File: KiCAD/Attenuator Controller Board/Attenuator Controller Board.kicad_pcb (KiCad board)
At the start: 2 copper layers, 100 x 70 mm, 30 parts, among them J1 Barrel_Jack_Switch, J2 Conn_Coaxial, J3 Conn_Coaxial, J4 Conn_01x24_Female, J5 DSub_15_HD, J6 DSub9, J7 DSub9, J8 DSub9, J9 Conn_01x24_Female, U1 RU_28_ADI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

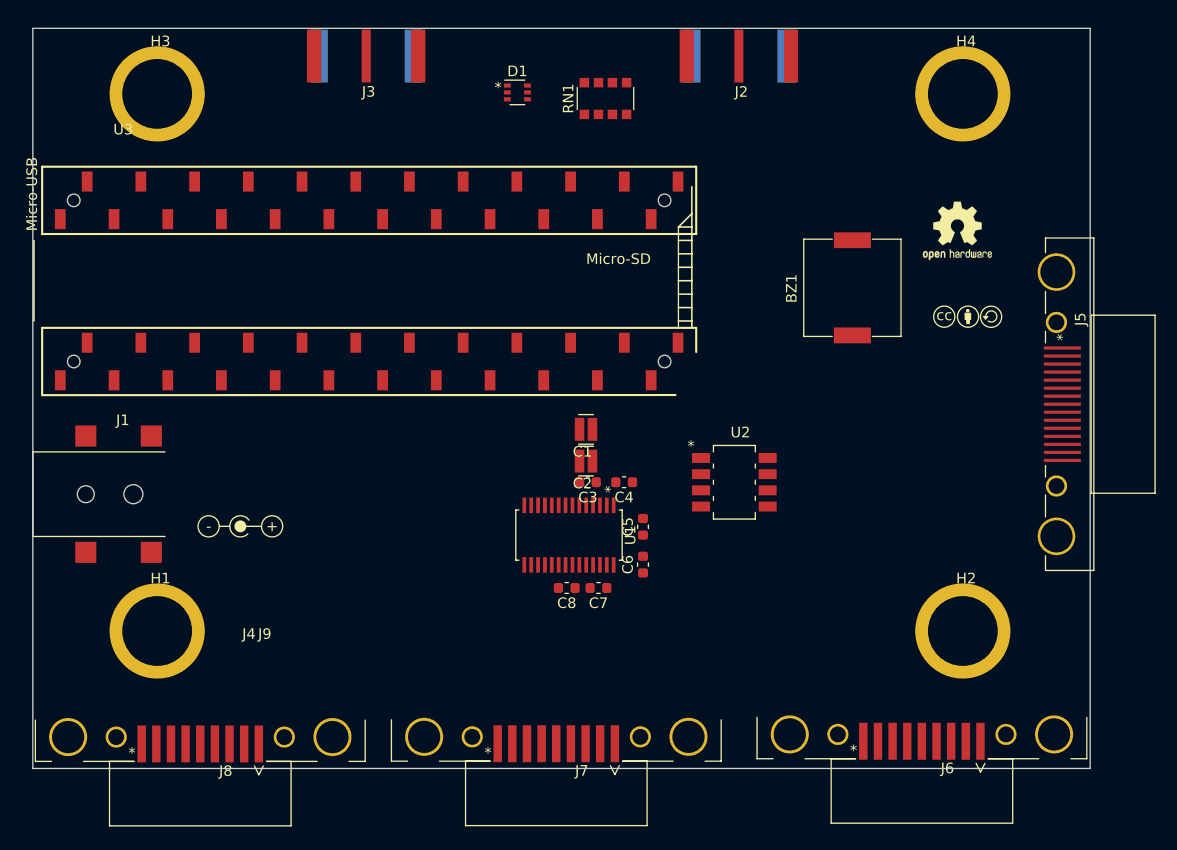
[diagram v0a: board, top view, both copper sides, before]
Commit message: Schottky diode protecting Vin->motor added
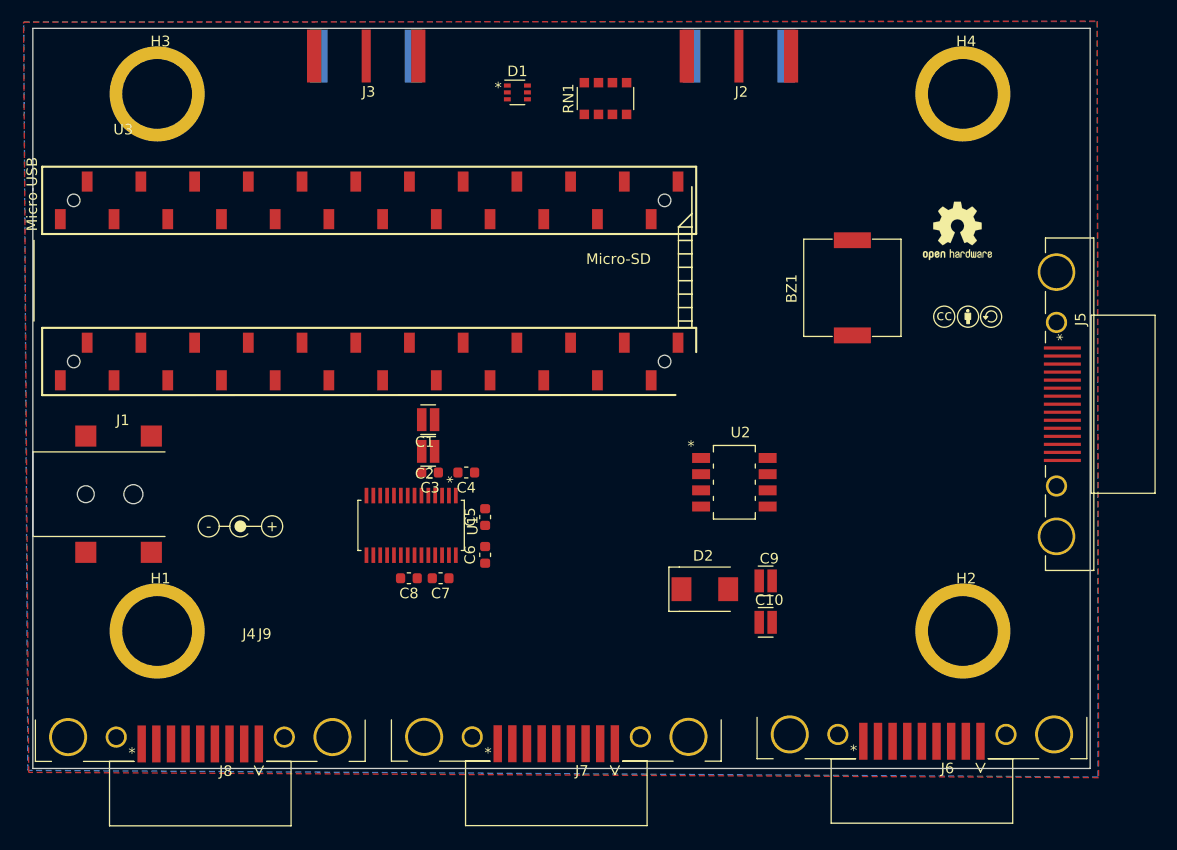
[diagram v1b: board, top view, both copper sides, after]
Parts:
- added C10: 10µF, Custom Footprints:0508_Capacitor, F.Cu at (169.3, 126.2)
- added C9: 10µF, Custom Footprints:0508_Capacitor, F.Cu at (169.3, 122.3)
- added D2: D_Schottky, Custom Footprints:DO-214BA, F.Cu at (163.6, 123.0)
- moved C1 15.0 mm to (137.4, 107.0)
- moved C2 15.0 mm to (137.4, 110.0)
- moved C3 15.0 mm to (137.6, 112.0)
- moved C4 15.0 mm to (141.0, 112.0)
- moved C5 15.0 mm to (142.8, 116.2)
- moved C6 15.0 mm to (142.8, 119.8)
- moved C7 15.0 mm to (138.6, 122.0)
- moved C8 15.0 mm to (135.6, 122.0)
- moved U1 15.0 mm to (135.8, 117.0)
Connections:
- U2 pad 6: /5V -> Net-(C10-Pad1)
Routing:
- added copper zone on B.Cu, net GND
- added copper zone on F.Cu, net GND

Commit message: Started on traces
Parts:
- U1: value RU_28_ADI -> ADM3307EARUZ
- U2: value SOIC_7T8TA_DIO -> ZXMHC3A01T8TA
- moved J8 68.3 mm to (184.1, 139.3)
- moved J6 68.2 mm to (115.9, 139.3)
- moved C1 4.34 mm to (137.6, 111.3)
- moved C4 4.28 mm to (139.9, 116.2)
- moved C3 4.19 mm to (137.0, 116.2)
- moved C2 4.05 mm to (137.6, 114.1)
- moved C5 3.98 mm to (140.8, 119.7)
- moved U1 3.80 mm to (134.9, 120.7)
- moved C6 3.49 mm to (140.8, 122.7), turned to 270 degrees
- moved C7 3.26 mm to (138.7, 125.3)
- moved C8 3.25 mm to (135.7, 125.3)
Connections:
- U1 pad 15: /RS-232_RXD3 -> /RS-232_RXD1
- U1 pad 17: /RS-232_RXD1 -> /RS-232_RXD3
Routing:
- net GND: track 0.00 -> 54.1 mm
- net /5V: track 0.00 -> 30.7 mm
- net /Gate3-4: track 0.00 -> 20.8 mm
- net /Gate1-2: track 0.00 -> 19.6 mm
- net /3v3: track 0.00 -> 16.4 mm
- net Net-(C6-Pad2): track 0.00 -> 10.3 mm
- net Net-(C5-Pad1): track 0.00 -> 5.25 mm
- net Net-(C5-Pad2): track 0.00 -> 4.20 mm
- net Net-(C6-Pad1): track 0.00 -> 4.19 mm
- net Net-(C4-Pad1): track 0.00 -> 2.39 mm
- net Net-(C7-Pad1): track 0.00 -> 2.15 mm
- net Net-(C7-Pad2): track 0.00 -> 2.03 mm
- net Net-(C8-Pad1): track 0.00 -> 1.76 mm

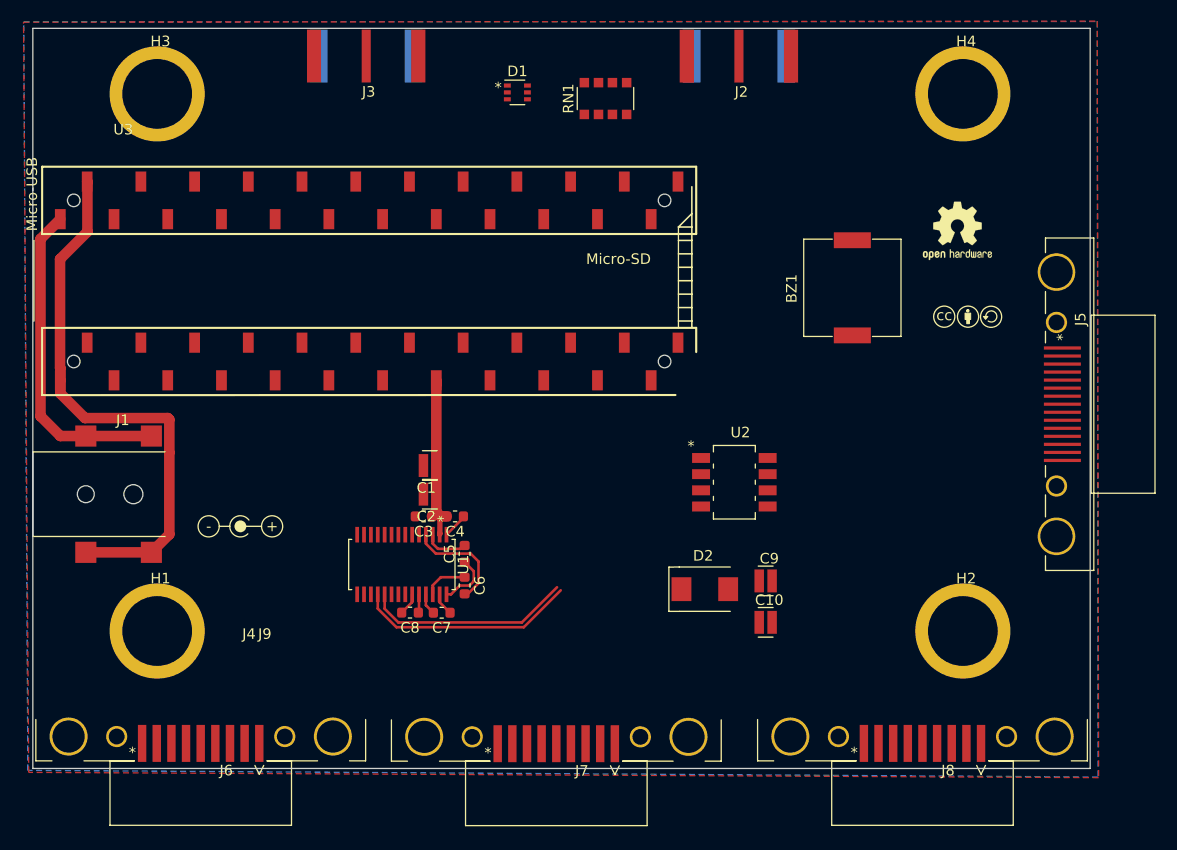
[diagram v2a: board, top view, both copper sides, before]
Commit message: RS-232 outs connected and shielded
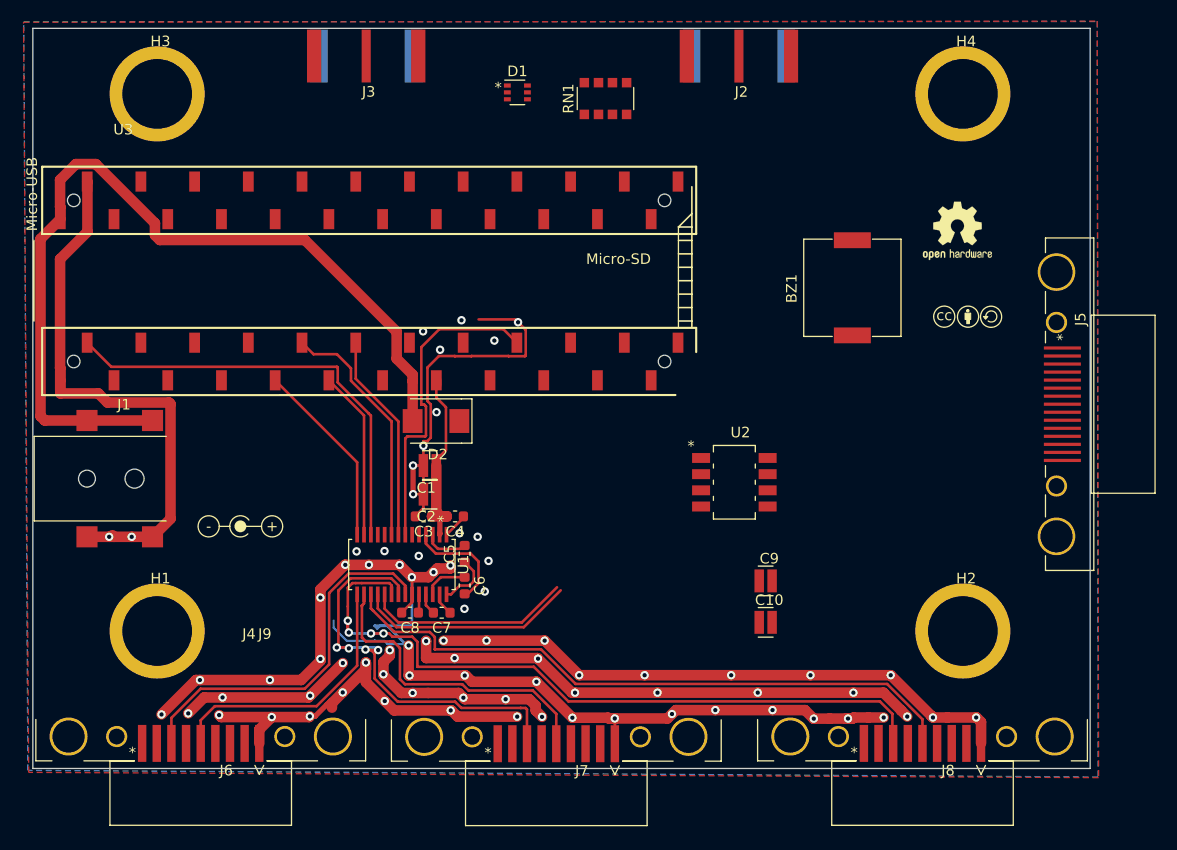
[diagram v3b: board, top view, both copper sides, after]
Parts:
- moved D2 30.0 mm to (138.1, 107.1), turned to 180 degrees
- moved J1 1.47 mm to (100.1, 112.6)
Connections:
- U3 pad 19: /Serial1-RX -> /NC27
- U3 pad 2: /Gate1-2 -> /Serial1-RX
- U3 pad 21: /NC29 -> /Enable
- U3 pad 22: /NC30 -> /Shutdown
- U3 pad 3: /Gate3-4 -> /NC1
- U3 pad 4: /Enable -> Net-(J4-Pad~)
- U3 pad 5: /Shutdown -> /Motor1
- U3 pad 7: /Encoder(A) -> /Motor2
- U3 pad 8: /Encoder(B) -> Net-(J4-Pad~)
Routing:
- net GND: track 54.1 -> 383.1 mm, vias 0 -> 78
- net /RS-232_TXD3: track 0.00 -> 72.0 mm, vias 0 -> 4
- net /RS-232_RXD3: track 0.00 -> 60.8 mm
- net /5V: track 30.7 -> 82.7 mm
- net /RS-232_TXD2: track 0.00 -> 42.3 mm, vias 0 -> 4
- net /Serial1-RX: track 0.00 -> 41.8 mm
- net /RS-232_TXD1: track 0.00 -> 35.4 mm
- net /RS-232_RXD2: track 0.00 -> 30.2 mm
- net /Serial1-TX: track 0.00 -> 30.1 mm
- net /RS-232_RXD1: track 0.00 -> 25.9 mm
- net /Serial3-TX: track 0.00 -> 23.0 mm
- net /Serial2-TX: track 0.00 -> 19.8 mm
- net /Serial3-RX: track 0.00 -> 17.8 mm
- net /Serial2-RX: track 0.00 -> 16.0 mm
- net /3v3: track 16.4 -> 18.5 mm

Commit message: Keep SD and EN low to keep RS-232 driver always on
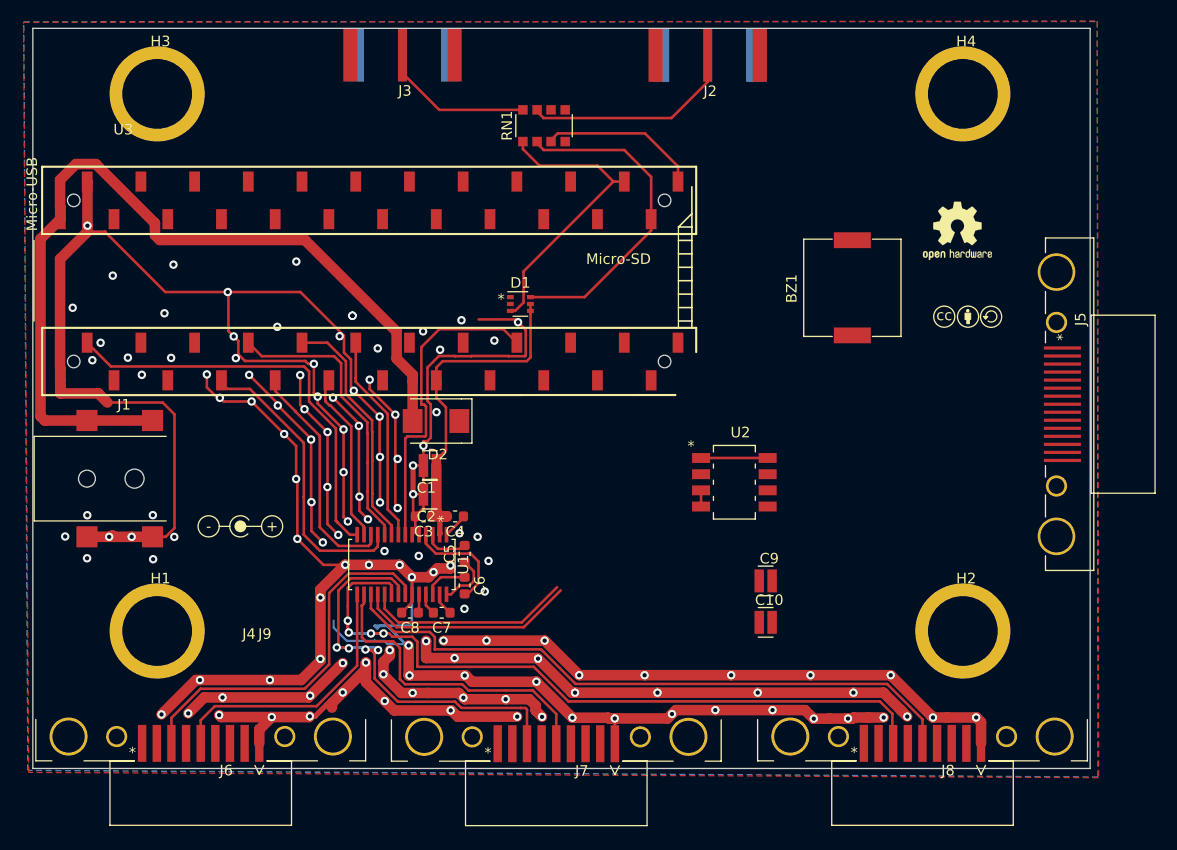
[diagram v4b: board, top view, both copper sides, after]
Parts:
- moved D1 20.0 mm to (146.1, 96.1)
- moved RN1 6.35 mm to (148.3, 79.2)
- moved J3 3.43 mm to (135.0, 72.5)
- moved J2 2.95 mm to (163.8, 72.6)
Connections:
- D1 pad 4: /3.3V -> /3v3
- D1 pad 5: /3.3V -> /3v3
- RN1 pad 1: /Analog_Input1 -> /Analog_Input2
- RN1 pad 2: /Analog_Input2 -> /Analog_Input1
- RN1 pad 3: GND -> /Ident(-)
- RN1 pad 6: /Ident(-) -> GND
- RN1 pad 7: Net-(J3-Pad1) -> Net-(J2-Pad1)
- RN1 pad 8: Net-(J2-Pad1) -> Net-(J3-Pad1)
- U1 pad 12: /Serial1-RX -> /Serial3-RX
- U1 pad 14: /Serial3-RX -> /Serial1-RX
- U1 pad 5: /Enable -> GND
- U1 pad 6: /Shutdown -> GND
- U3 pad 21: /Enable -> GND
- U3 pad 22: /Shutdown -> GND
- U3 pad 23: /Ident(-) -> Net-(J4-Pad~)
- U3 pad 24: /Analog_Input2 -> Net-(J4-Pad~)
- U3 pad 30: /Analog_Input1 -> /Ident(-)
- U3 pad 31: /NC34 -> /Analog_Input1
- U3 pad 32: /NC35 -> /Analog_Input2
- U3 pad 4: Net-(J4-Pad~) -> /NC2
- U3 pad 5: /Motor1 -> /NC3
- U3 pad 8: Net-(J4-Pad~) -> /Motor1
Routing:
- net GND: track 383.1 -> 552.3 mm, vias 78 -> 135
- net /Analog_Input1: track 0.00 -> 31.4 mm
- net /Analog_Input2: track 0.00 -> 28.1 mm
- net /Motor2: track 0.00 -> 28.0 mm
- net /Motor1: track 0.00 -> 27.5 mm
- net Net-(J2-Pad1): track 0.00 -> 20.5 mm
- net /3v3: track 18.5 -> 34.6 mm
- net /Ident(-): track 0.00 -> 15.1 mm
- net Net-(J3-Pad1): track 0.00 -> 14.5 mm
- net /Gate3-4: track 20.8 -> 27.1 mm
- net /Serial3-RX: track 17.8 -> 22.2 mm
- net /Serial1-RX: track 41.8 -> 40.1 mm
- net /Gate1-2: track 19.6 -> 21.1 mm

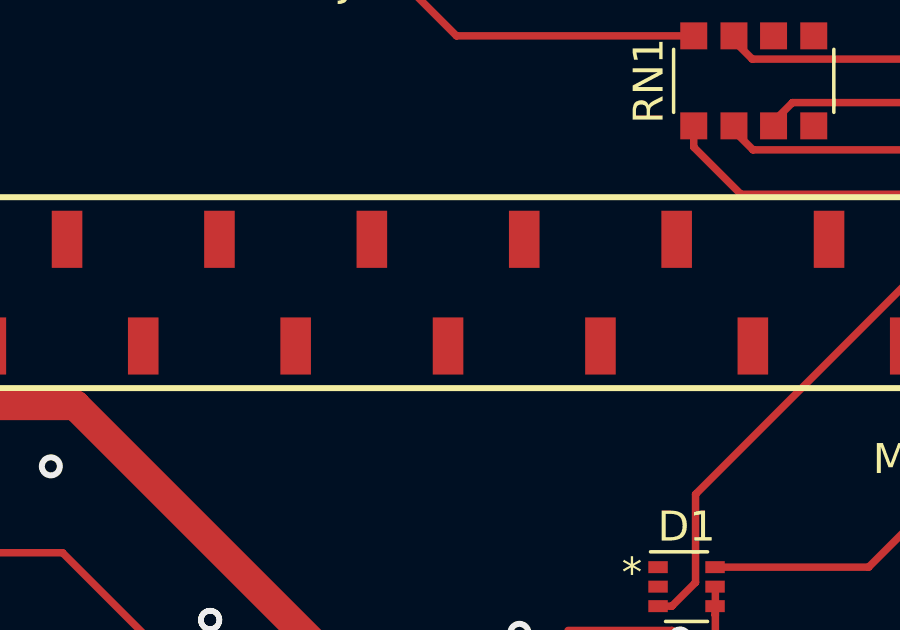
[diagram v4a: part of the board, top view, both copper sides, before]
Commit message: Disconnect SD and EN from Teensy
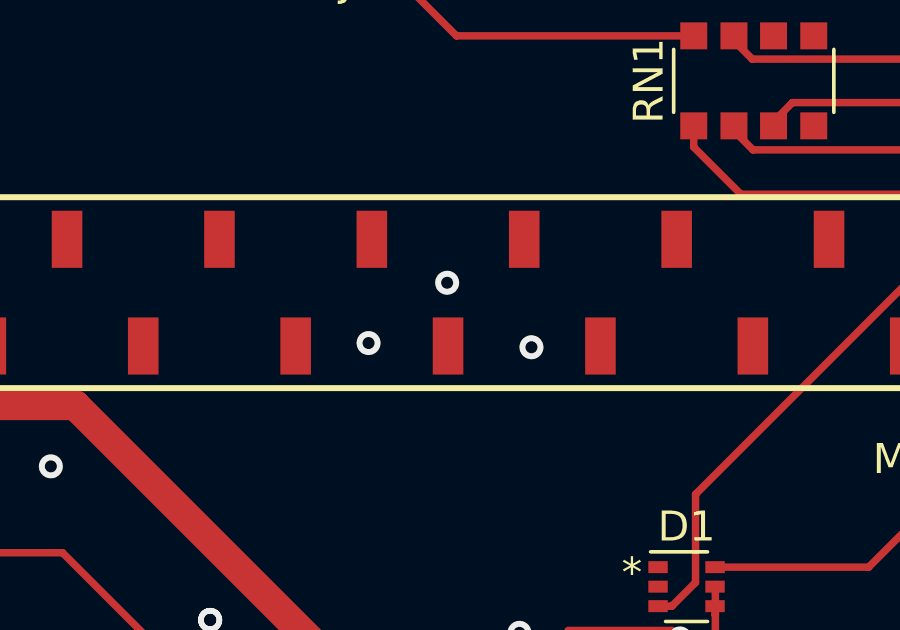
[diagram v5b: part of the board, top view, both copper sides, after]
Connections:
- U3 pad 21: GND -> Net-(J4-Pad~)
- U3 pad 22: GND -> Net-(J4-Pad~)
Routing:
- net GND: vias 135 -> 138
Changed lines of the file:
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@@
     (thickness 1.6)
     (drawings 4)
-    (tracks 726)
+    (tracks 729)
     (zones 0)
     (modules 33)
@@
       (net 88 "Net-(J4-Pad~)"))
     (pad 22 smd rect (at 24.13 -1.778) (size 1.02 1.905) (layers F.Cu F.Paste)
-      (net 4 GND))
+      (net 88 "Net-(J4-Pad~)"))
     (pad 21 smd rect (at 21.59 1.778) (size 1.02 1.905) (layers F.Cu F.Paste)
-      (net 4 GND))
+      (net 88 "Net-(J4-Pad~)"))
     (pad 20 smd rect (at 19.05 -1.778) (size 1.02 1.905) (layers F.Cu F.Paste)
       (net 65 /NC28))
@@
   (segment (start 135.97 115.955) (end 136.175 116.16) (width 0.25) (layer F.Cu) (net 4))
   (segment (start 135.97 114.06) (end 135.97 115.955) (width 0.25) (layer F.Cu) (net 4))
+  (via (at 138.13 85.94) (size 0.8) (drill 0.4) (layers F.Cu B.Cu) (net 4))
+  (via (at 135.51 87.95) (size 0.8) (drill 0.4) (layers F.Cu B.Cu) (net 4))
+  (via (at 140.94 88.09) (size 0.8) (drill 0.4) (layers F.Cu B.Cu) (net 4))
   (segment (start 140.725 116.2906) (end 139.125 117.8906) (width 0.25) (layer F.Cu) (net 5))
   (segment (start 140.725 116.16) (end 140.725 116.2906) (width 0.25) (layer F.Cu) (net 5))
